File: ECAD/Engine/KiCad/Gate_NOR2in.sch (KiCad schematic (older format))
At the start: 4 parts, among them Q493 2N7002, Q494 BSS84, Q495 BSS84, Q496 2N7002

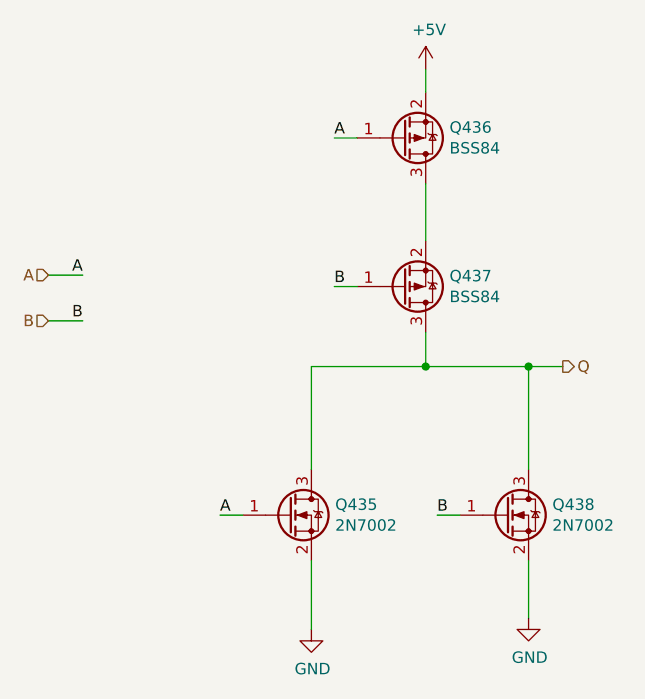
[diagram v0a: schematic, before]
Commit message: Engine: Added Tooling Holes, LCSC Part numbers
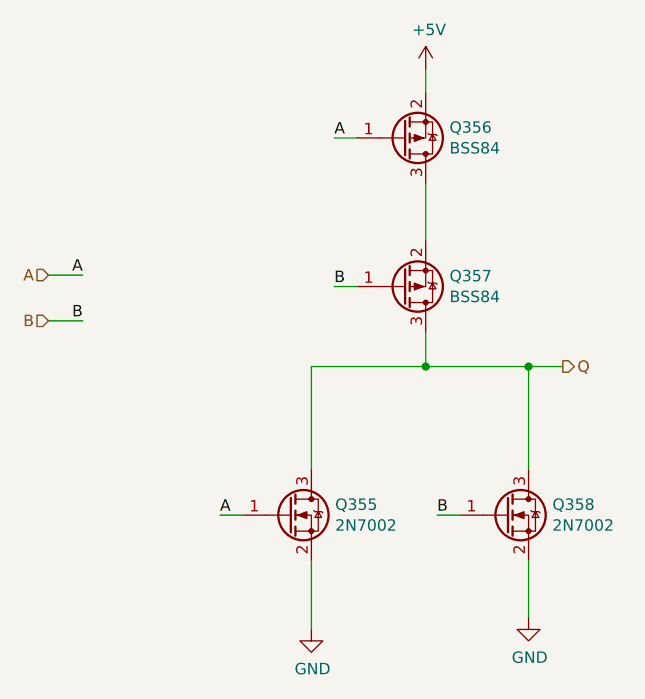
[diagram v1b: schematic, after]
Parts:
- Q493, Q496: LCSC (none) -> C8545
- Q494, Q495: LCSC (none) -> C114481
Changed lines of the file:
@@
 AR Path="/6073F2D8/606FFABF/60756041/60756040/5E557A8F" Ref="Q385"  Part="1"
 AR Path="/6073F2D8/606FFAC7/60756041/60756040/5E557A8F" Ref="Q399"  Part="1"
-F 0 "Q437" H 5304 2454 50  0000 L CNN
+F 0 "Q357" H 5304 2454 50  0000 L CNN
 F 1 "BSS84" H 5304 2545 50  0000 L CNN
 F 2 "LogicQ:SOT-23-P" H 5300 2600 50  0001 C CNN
 F 3 "~" H 5100 2500 50  0001 C CNN
+F 4 "C114481" H 5100 2500 50  0001 C CNN "LCSC"
 	1    5100 2500
 	1    0    0    1
@@
 AR Path="/6073F2D8/606FFABF/60756041/60756040/5E557A95" Ref="Q383"  Part="1"
 AR Path="/6073F2D8/606FFAC7/60756041/60756040/5E557A95" Ref="Q397"  Part="1"
-F 0 "Q435" H 4804 3546 50  0000 L CNN
+F 0 "Q355" H 4804 3546 50  0000 L CNN
 F 1 "2N7002" H 4804 3455 50  0000 L CNN
 F 2 "LogicQ:SOT-23-N" H 4800 3600 50  0001 C CNN
 F 3 "~" H 4600 3500 50  0001 C CNN
+F 4 "C8545" H 4600 3500 50  0001 C CNN "LCSC"
 	1    4600 3500
 	1    0    0    -1
@@
 AR Path="/6073F2D8/606FFABF/60756041/60756040/5E557A9B" Ref="Q384"  Part="1"
 AR Path="/6073F2D8/606FFAC7/60756041/60756040/5E557A9B" Ref="Q398"  Part="1"
-F 0 "Q436" H 5304 1804 50  0000 L CNN
+F 0 "Q356" H 5304 1804 50  0000 L CNN
 F 1 "BSS84" H 5304 1895 50  0000 L CNN
 F 2 "LogicQ:SOT-23-P" H 5300 1950 50  0001 C CNN
 F 3 "~" H 5100 1850 50  0001 C CNN
+F 4 "C114481" H 5100 1850 50  0001 C CNN "LCSC"
 	1    5100 1850
 	1    0    0    1
@@
 AR Path="/6073F2D8/606FFABF/60756041/60756040/5E557AA1" Ref="Q386"  Part="1"
 AR Path="/6073F2D8/606FFAC7/60756041/60756040/5E557AA1" Ref="Q400"  Part="1"
-F 0 "Q438" H 5754 3546 50  0000 L CNN
+F 0 "Q358" H 5754 3546 50  0000 L CNN
 F 1 "2N7002" H 5754 3455 50  0000 L CNN
 F 2 "LogicQ:SOT-23-N" H 5750 3600 50  0001 C CNN
 F 3 "~" H 5550 3500 50  0001 C CNN
+F 4 "C8545" H 5550 3500 50  0001 C CNN "LCSC"
 	1    5550 3500
 	1    0    0    -1
